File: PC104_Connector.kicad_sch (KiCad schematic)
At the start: 2 parts

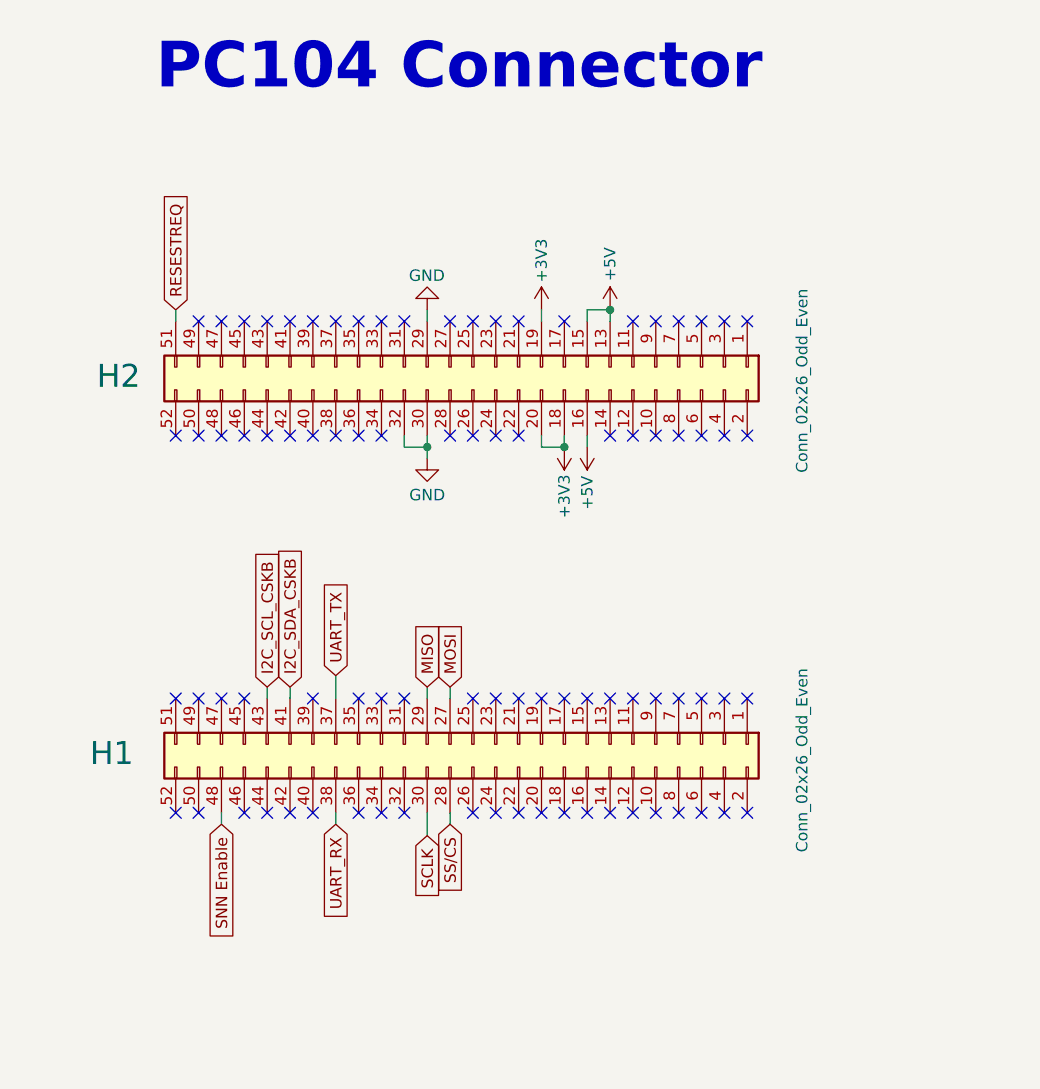
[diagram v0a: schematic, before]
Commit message: fixed and labeled CSKB header, added 3D models
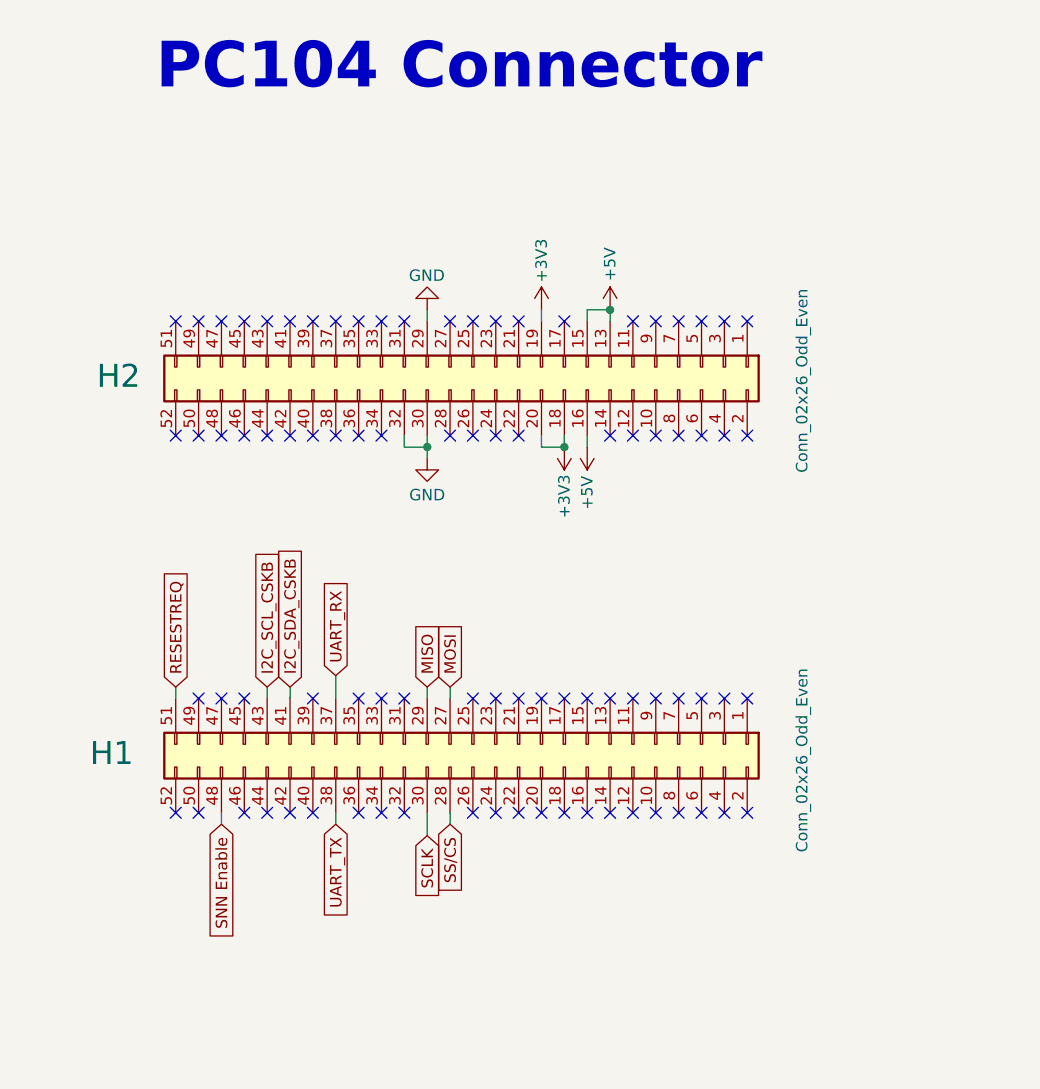
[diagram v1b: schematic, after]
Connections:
- net RESESTREQ: now also H1.51 (Pin_51); no longer H2.51 (Pin_51)
- net UART_RX: now also H1.37 (Pin_37); no longer H1.38 (Pin_38)
- net UART_TX: now also H1.38 (Pin_38); no longer H1.37 (Pin_37)
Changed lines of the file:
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@@
+	)
+	(no_connect
+		(at 113.03 50.8)
 	)
 	(no_connect
@@
 	)
 	(no_connect
-		(at 113.03 92.71)
-	)
-	(no_connect
 		(at 161.29 63.5)
 	)
@@
 	(wire
 		(pts
-			(xy 113.03 49.53) (xy 113.03 50.8)
+			(xy 113.03 91.44) (xy 113.03 92.71)
 		)
 		(stroke
@@
 	(global_label "RESESTREQ"
 		(shape input)
-		(at 113.03 49.53 90)
+		(at 113.03 91.44 90)
 		(fields_autoplaced yes)
 		(effects
@@
 		)
 		(property "Intersheetrefs" "${INTERSHEET_REFS}"
-			(at 113.03 35.8407 90)
+			(at 113.03 77.7507 90)
 			(effects
 				(font
@@
 	(global_label "UART_RX"
 		(shape input)
+		(at 130.81 90.17 90)
+		(fields_autoplaced yes)
+		(effects
+			(font
+				(size 1.27 1.27)
+			)
+			(justify left)
+		)
+		(property "Intersheetrefs" "${INTERSHEET_REFS}"
+			(at 130.81 79.081 90)
+			(effects
+				(font
+					(size 1.27 1.27)
+				)
+				(justify left)
+				(hide yes)
+			)
+		)
+	)
+	(global_label "UART_TX"
+		(shape input)
 		(at 130.81 106.68 270)
 		(fields_autoplaced yes)
@@
 		)
 		(property "Intersheetrefs" "${INTERSHEET_REFS}"
-			(at 130.81 117.769 90)
+			(at 130.81 117.4666 90)
 			(effects
 				(font
@@
 				(hide yes)
 			)
-		)
-	)
-	(global_label "UART_TX"
-		(shape input)
-		(at 130.81 90.17 90)
-		(fields_autoplaced yes)
-		(effects
-			(font
-				(size 1.27 1.27)
-			)
-			(justify left)
-		)
-		(property "Intersheetrefs" "${INTERSHEET_REFS}"
-			(at 130.81 79.3834 90)
-			(effects
-				(font
-					(size 1.27 1.27)
-				)
-				(justify left)
-				(hide yes)
-			)

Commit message: Fixed GND issues with connector and mounting holes
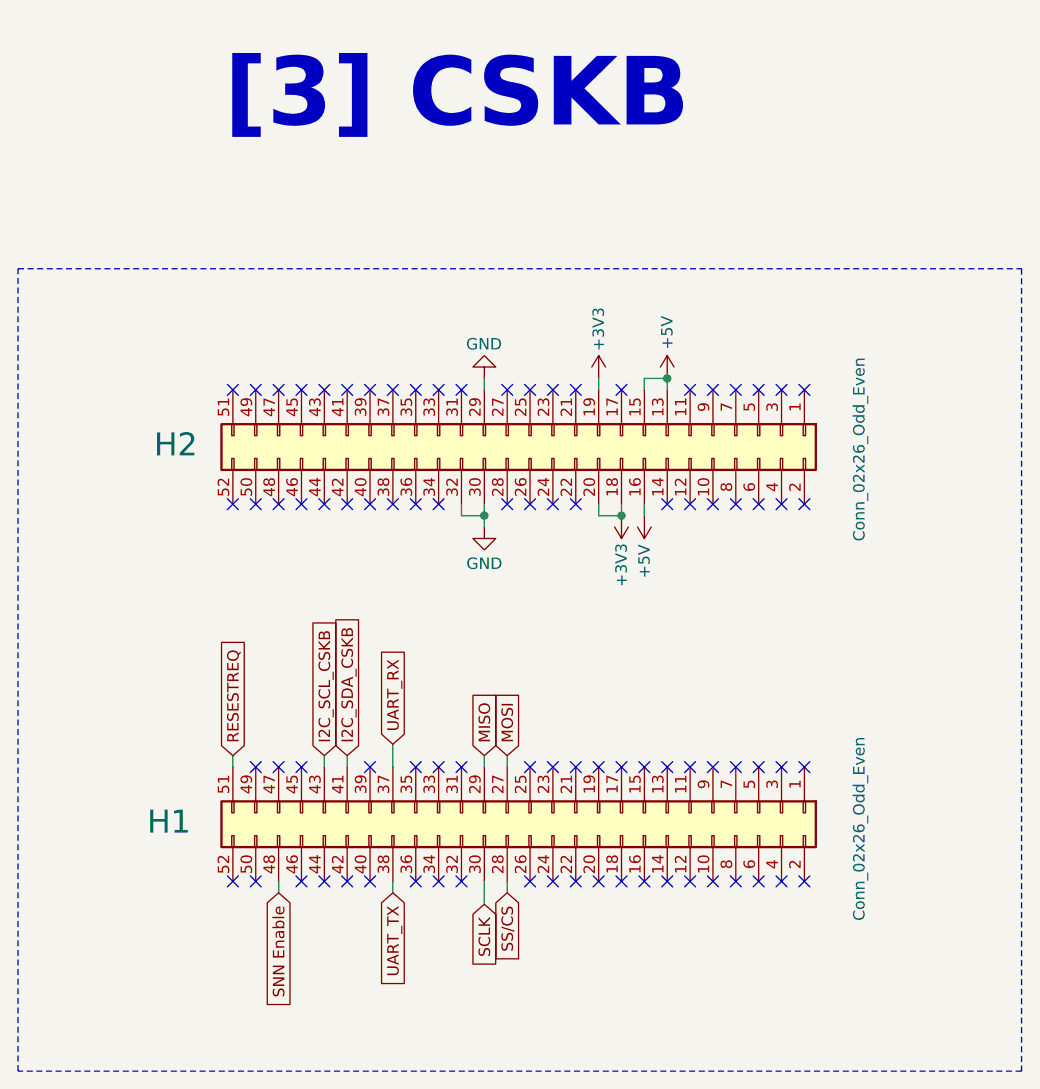
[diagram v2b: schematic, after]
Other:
- note added: "[3] CSKB"
- note removed: "PC104 Connector"
- moved on the sheet: H1, H2
